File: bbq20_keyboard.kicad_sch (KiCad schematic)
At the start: 41 parts, among them J1 Conn_Stemma_QT, J2 PMOD, J3 USB_C_Receptacle_USB2.0, U1 RP2040, U2 AP2112K-3.3, U3 GD25Q16xS, Y1 XYDBPCNANF-12MHZ

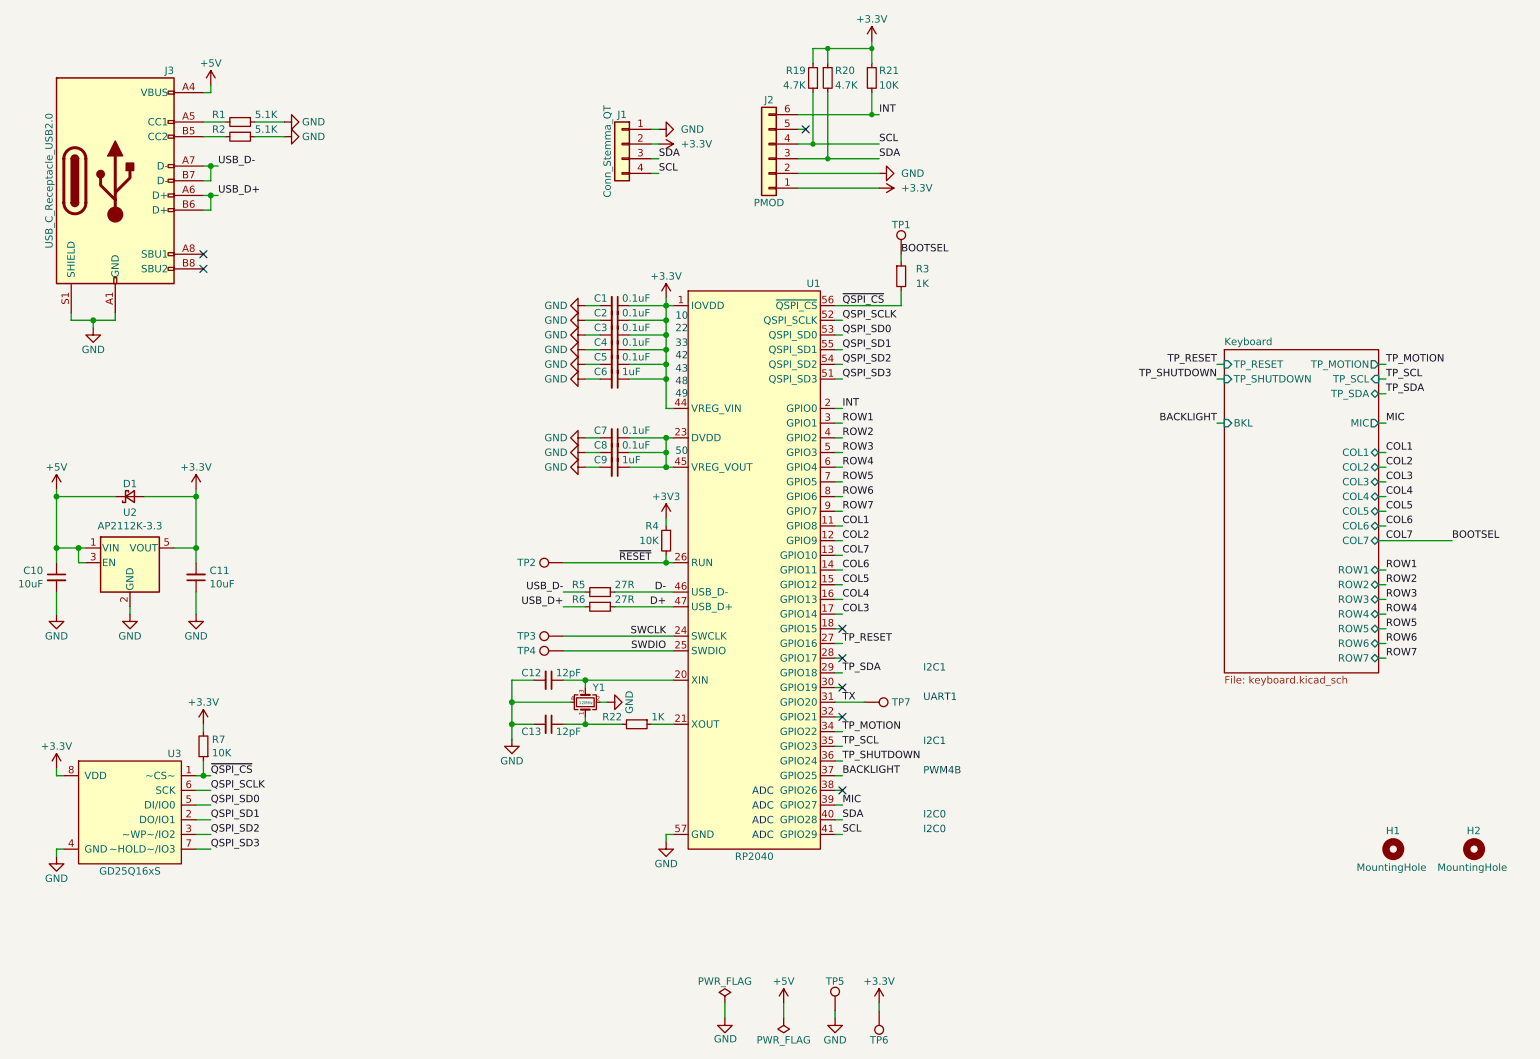
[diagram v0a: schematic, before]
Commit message: Migrate KiCAD version -> 1.0, update part numbers
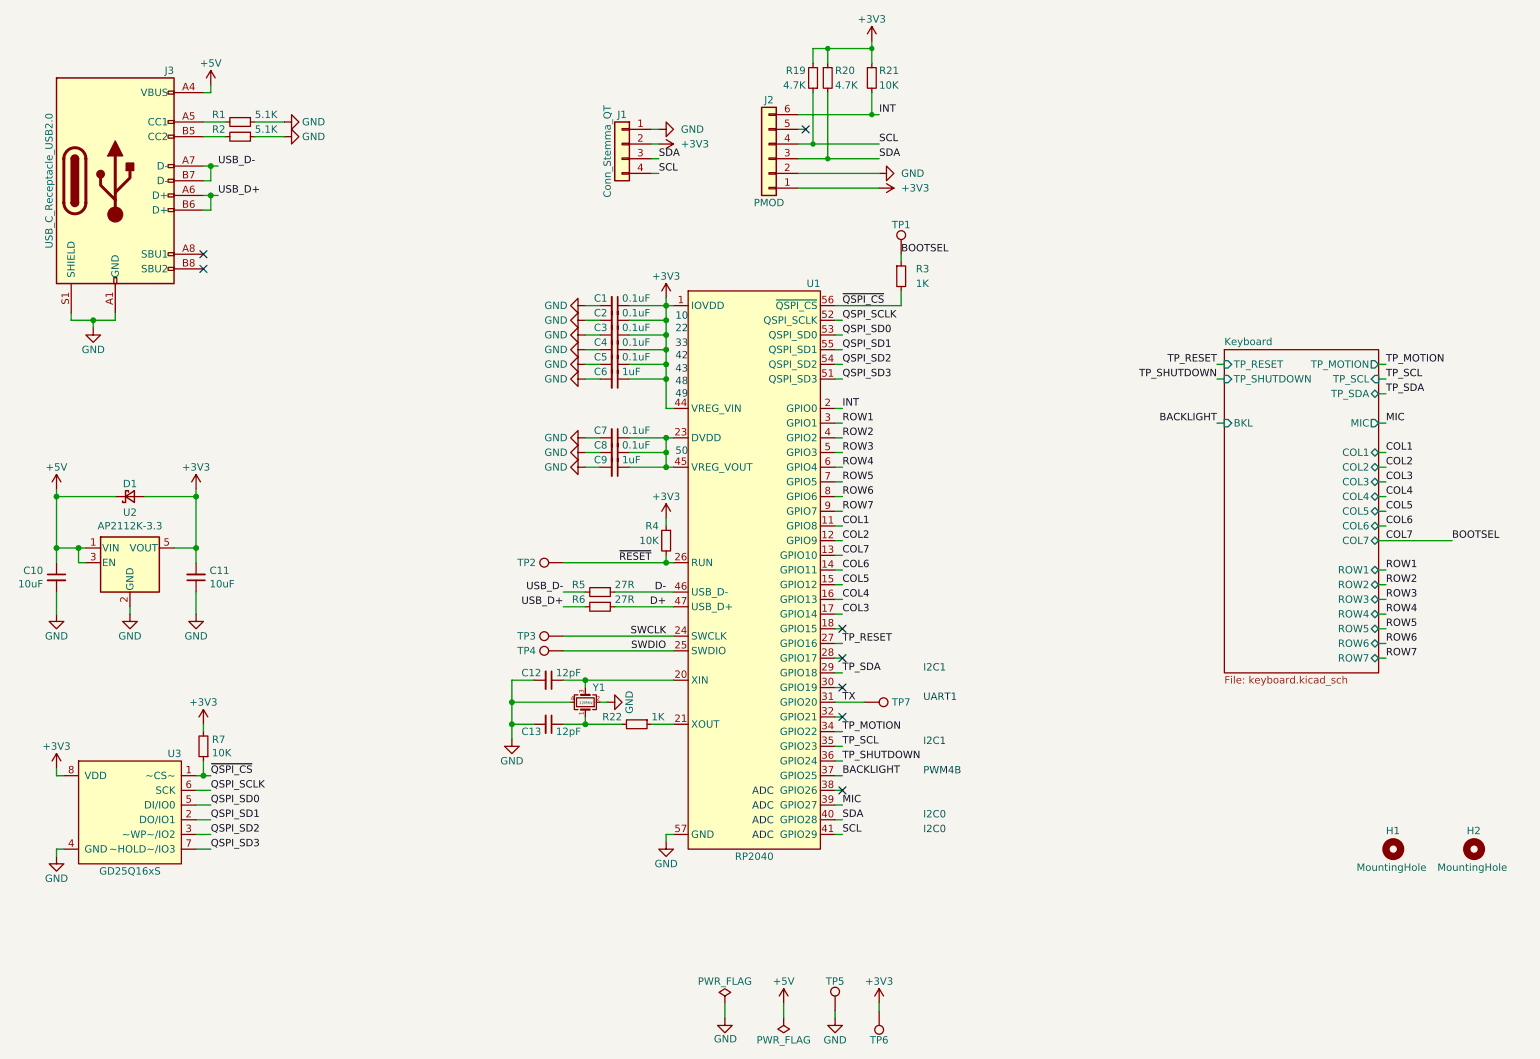
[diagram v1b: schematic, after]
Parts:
- H1, H2: now left out of the parts list
- J2: LCSC (none) -> C7501615
- U1: LCSC (none) -> C2040
- Y1: LCSC C709001 -> C521567
